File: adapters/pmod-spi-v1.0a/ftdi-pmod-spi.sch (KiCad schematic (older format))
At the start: 2 parts, among them J1 Conn, J4 Prog

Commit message: Updated the SPI PMOD adapter to a full PMOD interface.
This setup allows the use of the adapter with INT and RST lines too.
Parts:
- J4: value Prog -> PMOD; footprint Connector_PinSocket_2.54mm:PinSocket_1x06_P2.54mm_Vertical -> Connector_PinSocket_2.54mm:PinSocket_2x06_P2.54mm_Horizontal; symbol Connector_Generic:Conn_01x06 -> Connector_Generic:Conn_02x06_Odd_Even
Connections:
- net DI: now also J4.5 (Pin_5); no longer J4.3 (Pin_3)
- net DO: now also J4.3 (Pin_3); no longer J4.2 (Pin_2)
- net GND: now also J4.11 (Pin_11), J4.12 (Pin_12); no longer J4.6 (Pin_6)
- net GPIOL0: now also J4.2 (Pin_2)
- net GPIOL1: now also J4.4 (Pin_4)
- net SK: now also J4.7 (Pin_7); no longer J4.4 (Pin_4)
- no-connect marks 1 -> 4
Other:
- note added: "INT"
- note added: "RST"
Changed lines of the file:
@@
 	2700 1300 2700 2400
 $Comp
-L Connector_Generic:Conn_01x06 J4
+L Connector_Generic:Conn_02x06_Odd_Even J4
 U 1 1 5AB98614
 P 5000 1700
 F 0 "J4" H 4950 2000 50  0000 L CNN
-F 1 "Prog" H 4850 2100 50  0000 L CNN
-F 2 "Connector_PinSocket_2.54mm:PinSocket_1x06_P2.54mm_Vertical" H 5000 1700 50  0001 C CNN
+F 1 "PMOD" H 4850 2100 50  0000 L CNN
+F 2 "Connector_PinSocket_2.54mm:PinSocket_2x06_P2.54mm_Horizontal" H 5000 1700 50  0001 C CNN
 F 3 "~" H 5000 1700 50  0001 C CNN
 F 4 "ANY" H 5000 1700 50  0001 C CNN "Source"
@@
 	1    0    0    -1
 $EndComp
-Text Notes 5100 1600 0    50   ~ 0
+Text Notes 4450 1600 2    50   ~ 0
 MOSI
-Text Notes 5100 1700 0    50   ~ 0
+Text Notes 4450 1700 2    50   ~ 0
 MISO
-Text Notes 5100 1800 0    50   ~ 0
+Text Notes 4450 1800 2    50   ~ 0
 SCK
-Text Notes 5100 1500 0    50   ~ 0
+Text Notes 4450 1500 2    50   ~ 0
 CS
 Text Label 4600 1800 2    50   ~ 0
@@
 Text Label 4600 1500 2    50   ~ 0
 CS
+Wire Wire Line
+	5300 1500 5400 1500
+Wire Wire Line
+	5300 1600 5400 1600
+Wire Wire Line
+	5300 2000 5400 2000
+Wire Wire Line
+	5400 2000 5400 2100
+$Comp
+L power:GND #PWR0104
+U 1 1 5AAB3559
+P 5400 2100
+F 0 "#PWR0104" H 5400 1850 50  0001 C CNN
+F 1 "GND" H 5405 1924 50  0000 C CNN
+F 2 "" H 5400 2100 50  0001 C CNN
+F 3 "" H 5400 2100 50  0001 C CNN
+	1    5400 2100
+	1    0    0    -1
+$EndComp
+NoConn ~ 5300 1900
+NoConn ~ 5300 1700
+NoConn ~ 5300 1800
+Text Label 5400 1500 0    50   ~ 0
+GPIOL0
+Text Label 5400 1600 0    50   ~ 0
+GPIOL1
+Text Notes 5700 1500 0    50   ~ 0
+INT
+Text Notes 5700 1600 0    50   ~ 0
+RST
 $EndSCHEMATC

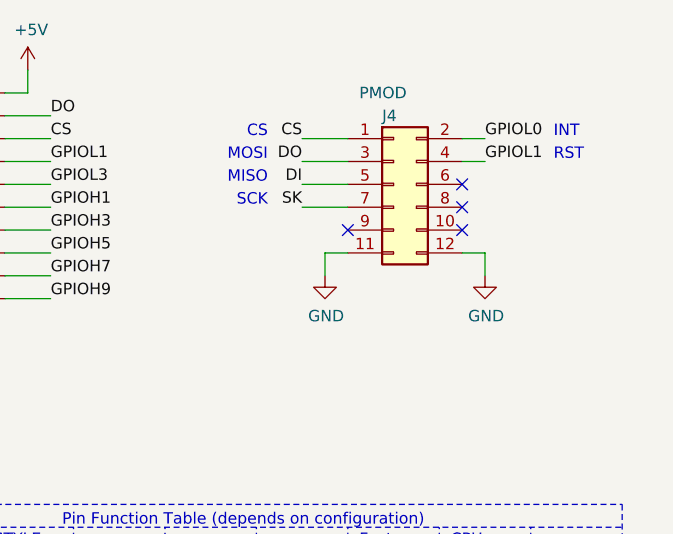
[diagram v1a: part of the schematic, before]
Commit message: Fixed PMOD pinout on SPI adapter.
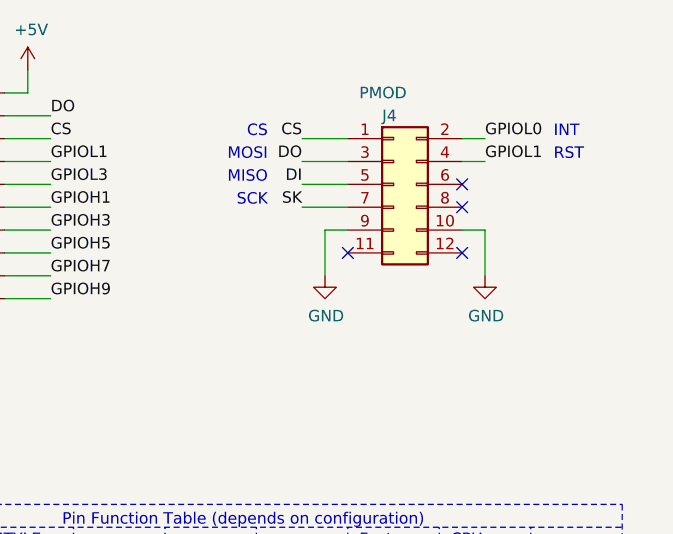
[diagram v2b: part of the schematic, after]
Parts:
- J4: footprint Connector_PinSocket_2.54mm:PinSocket_2x06_P2.54mm_Horizontal -> Connector_PinHeader_2.54mm:PinHeader_2x06_P2.54mm_Horizontal
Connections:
- net GND: now also J4.10 (Pin_10), J4.9 (Pin_9); no longer J4.11 (Pin_11), J4.12 (Pin_12)
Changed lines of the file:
@@
 F 0 "J4" H 4950 2000 50  0000 L CNN
 F 1 "PMOD" H 4850 2100 50  0000 L CNN
-F 2 "Connector_PinSocket_2.54mm:PinSocket_2x06_P2.54mm_Horizontal" H 5000 1700 50  0001 C CNN
+F 2 "Connector_PinHeader_2.54mm:PinHeader_2x06_P2.54mm_Horizontal" H 5000 1700 50  0001 C CNN
 F 3 "~" H 5000 1700 50  0001 C CNN
 F 4 "ANY" H 5000 1700 50  0001 C CNN "Source"
@@
 	4800 1800 4600 1800
 Wire Wire Line
-	4800 2000 4700 2000
+	4800 1900 4700 1900
 Text Label 4600 1600 2    50   ~ 0
 DO
@@
 DI
 Wire Wire Line
-	4700 2000 4700 2100
+	4700 1900 4700 2100
 $Comp
 L power:GND #PWR0103
@@
 Text Label 4600 1800 2    50   ~ 0
 SK
-NoConn ~ 4800 1900
+NoConn ~ 4800 2000
 Text Label 4600 1500 2    50   ~ 0
 CS
@@
 	5300 1600 5400 1600
 Wire Wire Line
-	5300 2000 5400 2000
+	5300 1900 5400 1900
 Wire Wire Line
-	5400 2000 5400 2100
+	5400 1900 5400 2100
 $Comp
 L power:GND #PWR0104
@@
 	1    0    0    -1
 $EndComp
-NoConn ~ 5300 1900
+NoConn ~ 5300 2000
 NoConn ~ 5300 1700
 NoConn ~ 5300 1800

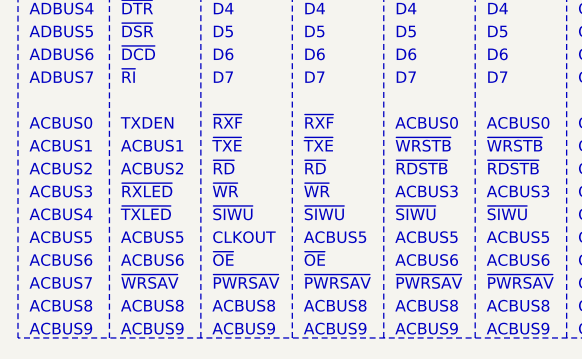
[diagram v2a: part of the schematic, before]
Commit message: A bunch of minor fixes.
* PWRSAV instead of WRSAV in signal table.
* 0.05 solder stop opening instead of 0.2
* Better copper fill parameters.
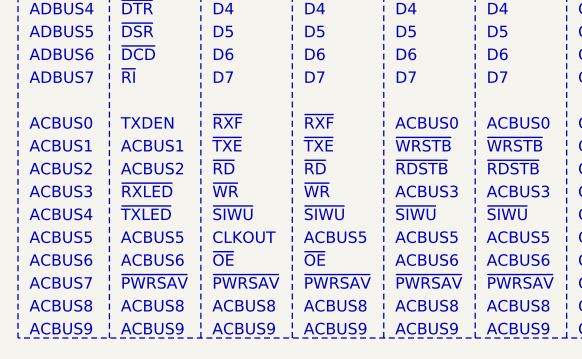
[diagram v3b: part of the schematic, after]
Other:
- note removed: "~WRSAV"
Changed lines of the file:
@@
 ACBUS8
 Text Notes 2450 5150 0    50   ~ 0
-~WRSAV
+~PWRSAV
 Text Notes 2450 5050 0    50   ~ 0
 ACBUS6
